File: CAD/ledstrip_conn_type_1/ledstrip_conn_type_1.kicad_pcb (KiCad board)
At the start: 2 copper layers, 22.3 x 19.3 mm, 4 parts, among them J1 led_strip_output, J2 led_strip_input, J3 led_strip_input

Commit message: Feat: Library mess fixed
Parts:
- J1: footprint led_strip_lib:strip_print_output -> ledstrip_footprints:strip_print_output
- J2, J3: footprint led_strip_lib:strip_print_input -> ledstrip_footprints:strip_print_input
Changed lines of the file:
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@@
     (fp_arc (start -5 -10) (mid -6.398026 -3.693905) (end -11.16025 0.66987) (layer "F.SilkS") (width 0.12))
     (fp_arc (start -6.16025 9.33013) (mid 0 7.387811) (end 6.16025 9.33013) (layer "F.SilkS") (width 0.12))
-    (fp_arc (start 11.16025 0.66987) (mid 6.398021 -3.693904) (end 5 -10) (layer "F.SilkS") (width 0.12))
+    (fp_arc (start 11.16025 0.66987) (mid 6.398025 -3.693904) (end 5 -10) (layer "F.SilkS") (width 0.12))
     (pad "1" thru_hole circle (at 0 -10) (size 2.3 2.3) (drill 1.7) (layers *.Cu *.Mask))
     (pad "2" thru_hole circle (at 2.5 -10) (size 2.3 2.3) (drill 1.7) (layers *.Cu *.Mask))
@@
     (pad "9" thru_hole circle (at -9.91025 2.83494) (size 2.3 2.3) (drill 1.7) (layers *.Cu *.Mask))
   )
-  (footprint "led_strip_lib:strip_print_output" (layer "F.Cu")
+  (footprint "ledstrip_footprints:strip_print_output" (layer "F.Cu")
     (at 159 77.55)
-    (property "Sheetfile" "")
+    (property "Sheetfile" "ledstrip_conn_type_1.kicad_sch")
     (property "Sheetname" "")
     (attr through_hole)
-    (fp_text reference "J1" (at -1.5 6 unlocked) (layer "F.SilkS")
+    (fp_text reference "J1" (at -1 7.5 unlocked) (layer "F.SilkS")
       (effects (font (size 1 1) (thickness 0.15)))
     )
@@
       (effects (font (size 1 1) (thickness 0.15)))
     )
-    (fp_text user "${REFERENCE}" (at -1.5 6 unlocked) (layer "F.Fab")
+    (fp_text user "V" (at 2.5 6 unlocked) (layer "F.SilkS")
       (effects (font (size 1 1) (thickness 0.15)))
     )
-    (pad "1" thru_hole circle (at 2.5 2) (size 2 2) (drill 0.4) (layers *.Cu *.Mask)
-      (net 1 "Net-(J1-Pad1)") (pinfunction "V") (pintype "input"))
+    (fp_text user "D" (at 0 6 unlocked) (layer "F.SilkS")
+      (effects (font (size 1 1) (thickness 0.15)))
+    )
+    (fp_text user "G" (at -2.5 6 unlocked) (layer "F.SilkS")
+      (effects (font (size 1 1) (thickness 0.15)))
+    )
     (pad "1" thru_hole circle (at 2.5 4) (size 2 2) (drill 0.4) (layers *.Cu *.Mask)
       (net 1 "Net-(J1-Pad1)") (pinfunction "V") (pintype "input"))
     (pad "1" thru_hole rect (at 2.5 0) (size 2 5) (drill 1.3 (offset 0 2.5)) (layers *.Cu *.Mask)
       (net 1 "Net-(J1-Pad1)") (pinfunction "V") (pintype "input"))
-    (pad "2" thru_hole rect (at 0 0) (size 2 5) (drill 1.3 (offset 0 2.5)) (layers *.Cu *.Mask)
-      (net 2 "Net-(J1-Pad2)") (pinfunction "Dout") (pintype "input"))
+    (pad "1" thru_hole circle (at 2.5 2) (size 2 2) (drill 0.4) (layers *.Cu *.Mask)
+      (net 1 "Net-(J1-Pad1)") (pinfunction "V") (pintype "input"))
     (pad "2" thru_hole circle (at 0 4) (size 2 2) (drill 0.4) (layers *.Cu *.Mask)
       (net 2 "Net-(J1-Pad2)") (pinfunction "Dout") (pintype "input"))
     (pad "2" thru_hole circle (at 0 2) (size 2 2) (drill 0.4) (layers *.Cu *.Mask)
+      (net 2 "Net-(J1-Pad2)") (pinfunction "Dout") (pintype "input"))
+    (pad "2" thru_hole rect (at 0 0) (size 2 5) (drill 1.3 (offset 0 2.5)) (layers *.Cu *.Mask)
       (net 2 "Net-(J1-Pad2)") (pinfunction "Dout") (pintype "input"))
     (pad "3" thru_hole circle (at -2.5 2) (size 2 2) (drill 0.4) (layers *.Cu *.Mask)
@@
       (net 3 "Net-(J1-Pad3)") (pinfunction "G") (pintype "input"))
   )
-  (footprint "led_strip_lib:strip_print_input" (layer "F.Cu")
+  (footprint "ledstrip_footprints:strip_print_input" (layer "F.Cu")
     (at 144.75 77.55)
-    (property "Sheetfile" "")
+    (property "Sheetfile" "ledstrip_conn_type_1.kicad_sch")
     (property "Sheetname" "")
     (attr through_hole)
-    (fp_text reference "J3" (at -1.5 6 unlocked) (layer "F.SilkS")
+    (fp_text reference "J3" (at -1.5 7.5 unlocked) (layer "F.SilkS")
       (effects (font (size 1 1) (thickness 0.15)))
     )
@@
       (effects (font (size 1 1) (thickness 0.15)))
     )
-    (fp_text user "${REFERENCE}" (at -1.5 6 unlocked) (layer "F.Fab")
+    (fp_text user "G" (at 2.5 6 unlocked) (layer "F.SilkS")
       (effects (font (size 1 1) (thickness 0.15)))
     )
+    (fp_text user "V" (at -2.5 6 unlocked) (layer "F.SilkS")
+      (effects (font (size 1 1) (thickness 0.15)))
+    )
+    (fp_text user "D" (at 0 6 unlocked) (layer "F.SilkS")
+      (effects (font (size 1 1) (thickness 0.15)))
+    )
+    (fp_text user "${REFERENCE}" (at -1.5 7.5 unlocked) (layer "F.Fab")
+      (effects (font (size 1 1) (thickness 0.15)))
+    )
+    (pad "1" thru_hole circle (at -2.5 2) (size 2 2) (drill 0.4) (layers *.Cu *.Mask)
+      (net 1 "Net-(J1-Pad1)") (pinfunction "V") (pintype "input"))
     (pad "1" thru_hole rect (at -2.5 0) (size 2 5) (drill 1.3 (offset 0 2.5)) (layers *.Cu *.Mask)
       (net 1 "Net-(J1-Pad1)") (pinfunction "V") (pintype "input"))
     (pad "1" thru_hole circle (at -2.5 4) (size 2 2) (drill 0.4) (layers *.Cu *.Mask)
       (net 1 "Net-(J1-Pad1)") (pinfunction "V") (pintype "input"))
-    (pad "1" thru_hole circle (at -2.5 2) (size 2 2) (drill 0.4) (layers *.Cu *.Mask)
-      (net 1 "Net-(J1-Pad1)") (pinfunction "V") (pintype "input"))
+    (pad "2" thru_hole circle (at 0 4) (size 2 2) (drill 0.4) (layers *.Cu *.Mask)
+      (net 2 "Net-(J1-Pad2)") (pinfunction "Din") (pintype "input"))
     (pad "2" thru_hole rect (at 0 0) (size 2 5) (drill 1.3 (offset 0 2.5)) (layers *.Cu *.Mask)
       (net 2 "Net-(J1-Pad2)") (pinfunction "Din") (pintype "input"))
     (pad "2" thru_hole circle (at 0 2) (size 2 2) (drill 0.4) (layers *.Cu *.Mask)
       (net 2 "Net-(J1-Pad2)") (pinfunction "Din") (pintype "input"))
-    (pad "2" thru_hole circle (at 0 4) (size 2 2) (drill 0.4) (layers *.Cu *.Mask)
-      (net 2 "Net-(J1-Pad2)") (pinfunction "Din") (pintype "input"))
-    (pad "3" thru_hole circle (at 2.5 4) (size 2 2) (drill 0.4) (layers *.Cu *.Mask)
+    (pad "3" thru_hole circle (at 2.5 2) (size 2 2) (drill 0.4) (layers *.Cu *.Mask)
       (net 3 "Net-(J1-Pad3)") (pinfunction "G") (pintype "input"))
     (pad "3" thru_hole rect (at 2.5 0) (size 2 5) (drill 1.3 (offset 0 2.5)) (layers *.Cu *.Mask)
       (net 3 "Net-(J1-Pad3)") (pinfunction "G") (pintype "input"))
-    (pad "3" thru_hole circle (at 2.5 2) (size 2 2) (drill 0.4) (layers *.Cu *.Mask)
+    (pad "3" thru_hole circle (at 2.5 4) (size 2 2) (drill 0.4) (layers *.Cu *.Mask)
       (net 3 "Net-(J1-Pad3)") (pinfunction "G") (pintype "input"))
   )
-  (footprint "led_strip_lib:strip_print_input" (layer "F.Cu")
+  (footprint "ledstrip_footprints:strip_print_input" (layer "F.Cu")
     (at 145 87.5)
-    (property "Sheetfile" "")
+    (property "Sheetfile" "ledstrip_conn_type_1.kicad_sch")
     (property "Sheetname" "")
     (attr through_hole)
-    (fp_text reference "J2" (at -1.5 6 unlocked) (layer "F.SilkS")
+    (fp_text reference "J2" (at -1.5 7.5 unlocked) (layer "F.SilkS")
       (effects (font (size 1 1) (thickness 0.15)))
     )
@@
       (effects (font (size 1 1) (thickness 0.15)))
     )
-    (fp_text user "${REFERENCE}" (at -1.5 6 unlocked) (layer "F.Fab")
+    (fp_text user "V" (at -2.5 6 unlocked) (layer "F.SilkS")
+      (effects (font (size 1 1) (thickness 0.15)))
+    )
+    (fp_text user "D" (at 0 6 unlocked) (layer "F.SilkS")
+      (effects (font (size 1 1) (thickness 0.15)))
+    )
+    (fp_text user "G" (at 2.5 6 unlocked) (layer "F.SilkS")
+      (effects (font (size 1 1) (thickness 0.15)))
+    )
+    (fp_text user "${REFERENCE}" (at -1.5 7.5 unlocked) (layer "F.Fab")
       (effects (font (size 1 1) (thickness 0.15)))
     )
     (pad "1" thru_hole circle (at -2.5 4) (size 2 2) (drill 0.4) (layers *.Cu *.Mask)
       (net 1 "Net-(J1-Pad1)") (pinfunction "V") (pintype "input"))
+    (pad "1" thru_hole rect (at -2.5 0) (size 2 5) (drill 1.3 (offset 0 2.5)) (layers *.Cu *.Mask)
+      (net 1 "Net-(J1-Pad1)") (pinfunction "V") (pintype "input"))
     (pad "1" thru_hole circle (at -2.5 2) (size 2 2) (drill 0.4) (layers *.Cu *.Mask)
       (net 1 "Net-(J1-Pad1)") (pinfunction "V") (pintype "input"))
-    (pad "1" thru_hole rect (at -2.5 0) (size 2 5) (drill 1.3 (offset 0 2.5)) (layers *.Cu *.Mask)
-      (net 1 "Net-(J1-Pad1)") (pinfunction "V") (pintype "input"))
-    (pad "2" thru_hole rect (at 0 0) (size 2 5) (drill 1.3 (offset 0 2.5)) (layers *.Cu *.Mask)
-      (net 4 "unconnected-(J2-Pad2)") (pinfunction "Din") (pintype "input"))
     (pad "2" thru_hole circle (at 0 4) (size 2 2) (drill 0.4) (layers *.Cu *.Mask)
       (net 4 "unconnected-(J2-Pad2)") (pinfunction "Din") (pintype "input"))
     (pad "2" thru_hole circle (at 0 2) (size 2 2) (drill 0.4) (layers *.Cu *.Mask)
       (net 4 "unconnected-(J2-Pad2)") (pinfunction "Din") (pintype "input"))
-    (pad "3" thru_hole circle (at 2.5 2) (size 2 2) (drill 0.4) (layers *.Cu *.Mask)
-      (net 5 "unconnected-(J2-Pad3)") (pinfunction "G") (pintype "input"))
+    (pad "2" thru_hole rect (at 0 0) (size 2 5) (drill 1.3 (offset 0 2.5)) (layers *.Cu *.Mask)
+      (net 4 "unconnected-(J2-Pad2)") (pinfunction "Din") (pintype "input"))
     (pad "3" thru_hole circle (at 2.5 4) (size 2 2) (drill 0.4) (layers *.Cu *.Mask)
       (net 5 "unconnected-(J2-Pad3)") (pinfunction "G") (pintype "input"))
     (pad "3" thru_hole rect (at 2.5 0) (size 2 5) (drill 1.3 (offset 0 2.5)) (layers *.Cu *.Mask)
       (net 5 "unconnected-(J2-Pad3)") (pinfunction "G") (pintype "input"))
+    (pad "3" thru_hole circle (at 2.5 2) (size 2 2) (drill 0.4) (layers *.Cu *.Mask)
+      (net 5 "unconnected-(J2-Pad3)") (pinfunction "G") (pintype "input"))
   )

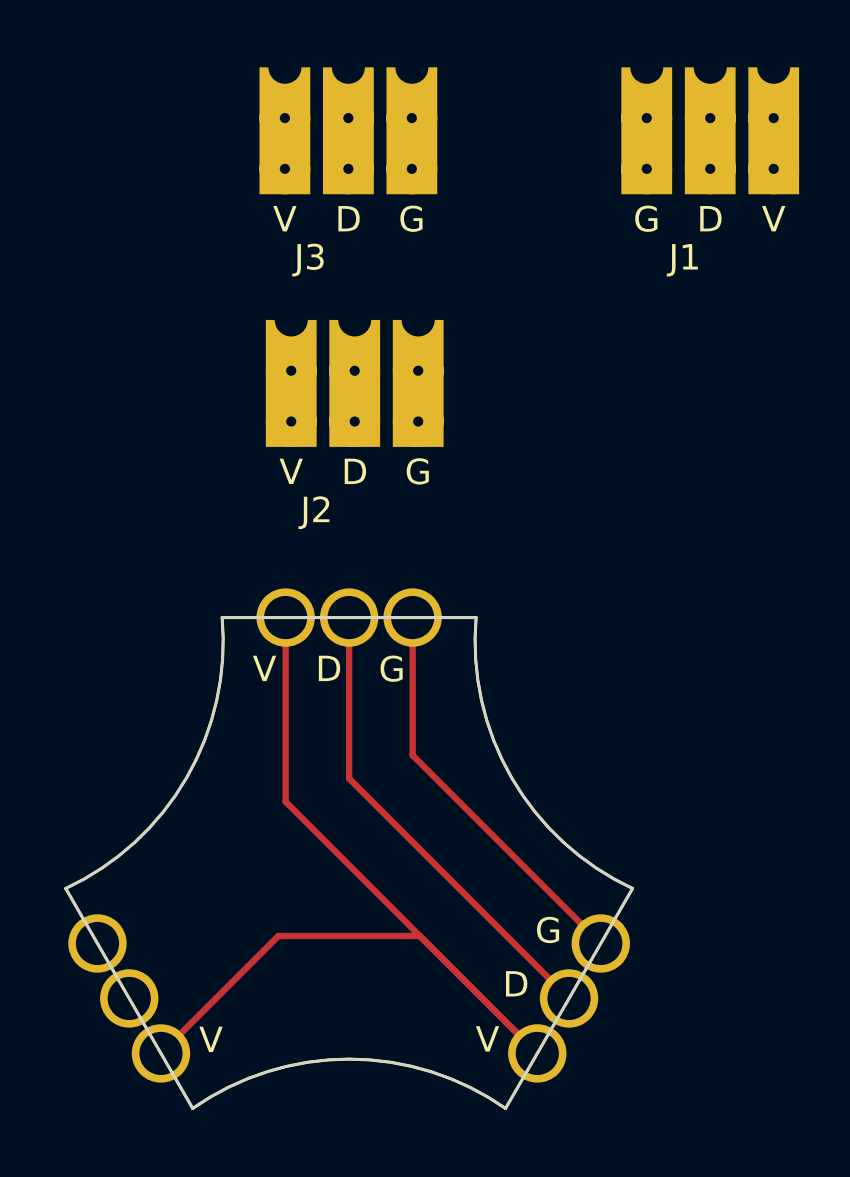
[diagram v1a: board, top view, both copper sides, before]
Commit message: fix: direction of ledstrips
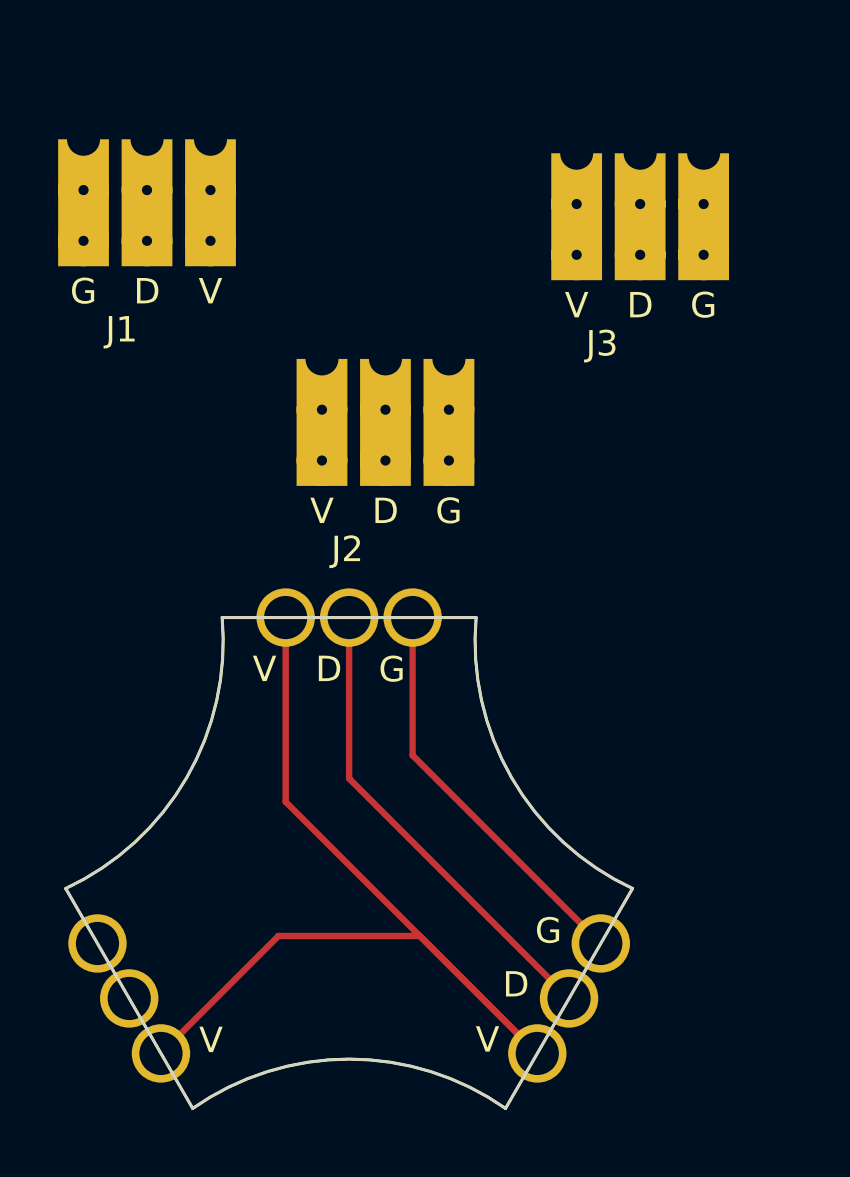
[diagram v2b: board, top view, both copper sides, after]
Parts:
- moved J1 22.4 mm to (136.8, 80.4)
- moved J3 12.0 mm to (156.2, 80.9)
- moved J2 1.95 mm to (146.2, 89.0)
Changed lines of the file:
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@@
   (net 4 "unconnected-(J2-Pad2)")
   (net 5 "unconnected-(J2-Pad3)")
+  (footprint "ledstrip_footprints:strip_print_input" (layer "F.Cu")
+    (at 156.24 80.935)
+    (property "Sheetfile" "ledstrip_conn_type_1.kicad_sch")
+    (property "Sheetname" "")
+    (attr through_hole)
+    (fp_text reference "J3" (at -1.5 7.5 unlocked) (layer "F.SilkS")
+      (effects (font (size 1 1) (thickness 0.15)))
+    )
+    (fp_text value "led_strip_input" (at 0 -2.5 unlocked) (layer "F.Fab")
+      (effects (font (size 1 1) (thickness 0.15)))
+    )
+    (fp_text user "D" (at 0 6 unlocked) (layer "F.SilkS")
+      (effects (font (size 1 1) (thickness 0.15)))
+    )
+    (fp_text user "G" (at 2.5 6 unlocked) (layer "F.SilkS")
+      (effects (font (size 1 1) (thickness 0.15)))
+    )
+    (fp_text user "V" (at -2.5 6 unlocked) (layer "F.SilkS")
+      (effects (font (size 1 1) (thickness 0.15)))
+    )
+    (fp_text user "${REFERENCE}" (at -1.5 7.5 unlocked) (layer "F.Fab")
+      (effects (font (size 1 1) (thickness 0.15)))
+    )
+    (pad "1" thru_hole circle (at -2.5 4) (size 2 2) (drill 0.4) (layers *.Cu *.Mask)
+      (net 1 "Net-(J1-Pad1)") (pinfunction "V") (pintype "input"))
+    (pad "1" thru_hole circle (at -2.5 2) (size 2 2) (drill 0.4) (layers *.Cu *.Mask)
+      (net 1 "Net-(J1-Pad1)") (pinfunction "V") (pintype "input"))
+    (pad "1" thru_hole rect (at -2.5 0) (size 2 5) (drill 1.3 (offset 0 2.5)) (layers *.Cu *.Mask)
+      (net 1 "Net-(J1-Pad1)") (pinfunction "V") (pintype "input"))
+    (pad "2" thru_hole circle (at 0 4) (size 2 2) (drill 0.4) (layers *.Cu *.Mask)
+      (net 2 "Net-(J1-Pad2)") (pinfunction "Din") (pintype "input"))
+    (pad "2" thru_hole rect (at 0 0) (size 2 5) (drill 1.3 (offset 0 2.5)) (layers *.Cu *.Mask)
+      (net 2 "Net-(J1-Pad2)") (pinfunction "Din") (pintype "input"))
+    (pad "2" thru_hole circle (at 0 2) (size 2 2) (drill 0.4) (layers *.Cu *.Mask)
+      (net 2 "Net-(J1-Pad2)") (pinfunction "Din") (pintype "input"))
+    (pad "3" thru_hole rect (at 2.5 0) (size 2 5) (drill 1.3 (offset 0 2.5)) (layers *.Cu *.Mask)
+      (net 3 "Net-(J1-Pad3)") (pinfunction "G") (pintype "input"))
+    (pad "3" thru_hole circle (at 2.5 2) (size 2 2) (drill 0.4) (layers *.Cu *.Mask)
+      (net 3 "Net-(J1-Pad3)") (pinfunction "G") (pintype "input"))
+    (pad "3" thru_hole circle (at 2.5 4) (size 2 2) (drill 0.4) (layers *.Cu *.Mask)
+      (net 3 "Net-(J1-Pad3)") (pinfunction "G") (pintype "input"))
+  )
   (footprint "Connector:led_cube" (layer "F.Cu")
     (at 144.78 109.22)
@@
   )
   (footprint "ledstrip_footprints:strip_print_output" (layer "F.Cu")
-    (at 159 77.55)
+    (at 136.82 80.385)
     (property "Sheetfile" "ledstrip_conn_type_1.kicad_sch")
     (property "Sheetname" "")
@@
       (effects (font (size 1 1) (thickness 0.15)))
     )
+    (fp_text user "G" (at -2.5 6 unlocked) (layer "F.SilkS")
+      (effects (font (size 1 1) (thickness 0.15)))
+    )
     (fp_text user "V" (at 2.5 6 unlocked) (layer "F.SilkS")
       (effects (font (size 1 1) (thickness 0.15)))
@@
       (effects (font (size 1 1) (thickness 0.15)))
     )
-    (fp_text user "G" (at -2.5 6 unlocked) (layer "F.SilkS")
-      (effects (font (size 1 1) (thickness 0.15)))
-    )
-    (pad "1" thru_hole circle (at 2.5 4) (size 2 2) (drill 0.4) (layers *.Cu *.Mask)
-      (net 1 "Net-(J1-Pad1)") (pinfunction "V") (pintype "input"))
     (pad "1" thru_hole rect (at 2.5 0) (size 2 5) (drill 1.3 (offset 0 2.5)) (layers *.Cu *.Mask)
       (net 1 "Net-(J1-Pad1)") (pinfunction "V") (pintype "input"))
     (pad "1" thru_hole circle (at 2.5 2) (size 2 2) (drill 0.4) (layers *.Cu *.Mask)
       (net 1 "Net-(J1-Pad1)") (pinfunction "V") (pintype "input"))
-    (pad "2" thru_hole circle (at 0 4) (size 2 2) (drill 0.4) (layers *.Cu *.Mask)
+    (pad "1" thru_hole circle (at 2.5 4) (size 2 2) (drill 0.4) (layers *.Cu *.Mask)
+      (net 1 "Net-(J1-Pad1)") (pinfunction "V") (pintype "input"))
+    (pad "2" thru_hole rect (at 0 0) (size 2 5) (drill 1.3 (offset 0 2.5)) (layers *.Cu *.Mask)
       (net 2 "Net-(J1-Pad2)") (pinfunction "Dout") (pintype "input"))
     (pad "2" thru_hole circle (at 0 2) (size 2 2) (drill 0.4) (layers *.Cu *.Mask)
       (net 2 "Net-(J1-Pad2)") (pinfunction "Dout") (pintype "input"))
-    (pad "2" thru_hole rect (at 0 0) (size 2 5) (drill 1.3 (offset 0 2.5)) (layers *.Cu *.Mask)
+    (pad "2" thru_hole circle (at 0 4) (size 2 2) (drill 0.4) (layers *.Cu *.Mask)
       (net 2 "Net-(J1-Pad2)") (pinfunction "Dout") (pintype "input"))
     (pad "3" thru_hole circle (at -2.5 2) (size 2 2) (drill 0.4) (layers *.Cu *.Mask)
@@
   )
   (footprint "ledstrip_footprints:strip_print_input" (layer "F.Cu")
-    (at 144.75 77.55)
+    (at 146.21 89.035)
     (property "Sheetfile" "ledstrip_conn_type_1.kicad_sch")
     (property "Sheetname" "")
     (attr through_hole)
-    (fp_text reference "J3" (at -1.5 7.5 unlocked) (layer "F.SilkS")
+    (fp_text reference "J2" (at -1.5 7.5 unlocked) (layer "F.SilkS")
       (effects (font (size 1 1) (thickness 0.15)))
     )
@@
       (net 1 "Net-(J1-Pad1)") (pinfunction "V") (pintype "input"))
     (pad "2" thru_hole circle (at 0 4) (size 2 2) (drill 0.4) (layers *.Cu *.Mask)
-      (net 2 "Net-(J1-Pad2)") (pinfunction "Din") (pintype "input"))
+      (net 4 "unconnected-(J2-Pad2)") (pinfunction "Din") (pintype "input"))
     (pad "2" thru_hole rect (at 0 0) (size 2 5) (drill 1.3 (offset 0 2.5)) (layers *.Cu *.Mask)
-      (net 2 "Net-(J1-Pad2)") (pinfunction "Din") (pintype "input"))
-    (pad "2" thru_hole circle (at 0 2) (size 2 2) (drill 0.4) (layers *.Cu *.Mask)
-      (net 2 "Net-(J1-Pad2)") (pinfunction "Din") (pintype "input"))
-    (pad "3" thru_hole circle (at 2.5 2) (size 2 2) (drill 0.4) (layers *.Cu *.Mask)
-      (net 3 "Net-(J1-Pad3)") (pinfunction "G") (pintype "input"))
-    (pad "3" thru_hole rect (at 2.5 0) (size 2 5) (drill 1.3 (offset 0 2.5)) (layers *.Cu *.Mask)
-      (net 3 "Net-(J1-Pad3)") (pinfunction "G") (pintype "input"))
-    (pad "3" thru_hole circle (at 2.5 4) (size 2 2) (drill 0.4) (layers *.Cu *.Mask)
-      (net 3 "Net-(J1-Pad3)") (pinfunction "G") (pintype "input"))
-  )
-  (footprint "ledstrip_footprints:strip_print_input" (layer "F.Cu")
-    (at 145 87.5)
-    (property "Sheetfile" "ledstrip_conn_type_1.kicad_sch")
-    (property "Sheetname" "")
-    (attr through_hole)
-    (fp_text reference "J2" (at -1.5 7.5 unlocked) (layer "F.SilkS")
-      (effects (font (size 1 1) (thickness 0.15)))
-    )
-    (fp_text value "led_strip_input" (at 0 -2.5 unlocked) (layer "F.Fab")
-      (effects (font (size 1 1) (thickness 0.15)))
-    )
-    (fp_text user "V" (at -2.5 6 unlocked) (layer "F.SilkS")
-      (effects (font (size 1 1) (thickness 0.15)))
-    )
-    (fp_text user "D" (at 0 6 unlocked) (layer "F.SilkS")
-      (effects (font (size 1 1) (thickness 0.15)))
-    )
-    (fp_text user "G" (at 2.5 6 unlocked) (layer "F.SilkS")
-      (effects (font (size 1 1) (thickness 0.15)))
-    )
-    (fp_text user "${REFERENCE}" (at -1.5 7.5 unlocked) (layer "F.Fab")
-      (effects (font (size 1 1) (thickness 0.15)))
-    )
-    (pad "1" thru_hole circle (at -2.5 4) (size 2 2) (drill 0.4) (layers *.Cu *.Mask)
-      (net 1 "Net-(J1-Pad1)") (pinfunction "V") (pintype "input"))
-    (pad "1" thru_hole rect (at -2.5 0) (size 2 5) (drill 1.3 (offset 0 2.5)) (layers *.Cu *.Mask)
-      (net 1 "Net-(J1-Pad1)") (pinfunction "V") (pintype "input"))
-    (pad "1" thru_hole circle (at -2.5 2) (size 2 2) (drill 0.4) (layers *.Cu *.Mask)
-      (net 1 "Net-(J1-Pad1)") (pinfunction "V") (pintype "input"))
-    (pad "2" thru_hole circle (at 0 4) (size 2 2) (drill 0.4) (layers *.Cu *.Mask)
       (net 4 "unconnected-(J2-Pad2)") (pinfunction "Din") (pintype "input"))
     (pad "2" thru_hole circle (at 0 2) (size 2 2) (drill 0.4) (layers *.Cu *.Mask)
       (net 4 "unconnected-(J2-Pad2)") (pinfunction "Din") (pintype "input"))
-    (pad "2" thru_hole rect (at 0 0) (size 2 5) (drill 1.3 (offset 0 2.5)) (layers *.Cu *.Mask)
-      (net 4 "unconnected-(J2-Pad2)") (pinfunction "Din") (pintype "input"))
-    (pad "3" thru_hole circle (at 2.5 4) (size 2 2) (drill 0.4) (layers *.Cu *.Mask)
-      (net 5 "unconnected-(J2-Pad3)") (pinfunction "G") (pintype "input"))
     (pad "3" thru_hole rect (at 2.5 0) (size 2 5) (drill 1.3 (offset 0 2.5)) (layers *.Cu *.Mask)
       (net 5 "unconnected-(J2-Pad3)") (pinfunction "G") (pintype "input"))
     (pad "3" thru_hole circle (at 2.5 2) (size 2 2) (drill 0.4) (layers *.Cu *.Mask)
       (net 5 "unconnected-(J2-Pad3)") (pinfunction "G") (pintype "input"))
+    (pad "3" thru_hole circle (at 2.5 4) (size 2 2) (drill 0.4) (layers *.Cu *.Mask)
+      (net 5 "unconnected-(J2-Pad3)") (pinfunction "G") (pintype "input"))
   )
